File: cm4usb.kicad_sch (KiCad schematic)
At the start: 24 parts, among them J6 USB4110-GF-A, J7 USB4110-GF-A, U10 USB3740B-AI2, U11 AP22653FDZ-7

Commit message: respin
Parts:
- renumbered C20 to C22, C21 to C23, C22 to C24, C23 to C25, C24 to C26, C25 to C27, C26 to C28, C27 to C29, C28 to C30, C29 to C31, D8 to D7, R25 to R28, R26 to R29, R27 to R30, R28 to R31, R29 to R32, R30 to R33, R31 to R34, R32 to R35, R33 to R36, U10 to U11, U11 to U12
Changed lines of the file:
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@@
   (symbol (lib_id "Device:R_Small") (at 297.434 85.344 270) (unit 1)
     (in_bom yes) (on_board yes)
-    (property "Reference" "R32" (id 0) (at 297.434 87.63 90))
+    (property "Reference" "R35" (id 0) (at 297.434 87.63 90))
     (property "Value" "10k" (id 1) (at 297.434 90.17 90))
     (property "Footprint" "Resistor_SMD:R_0402_1005Metric" (id 2) (at 297.434 85.344 0)
@@
   (symbol (lib_id "Device:R_Small") (at 203.2 254 90) (unit 1)
     (in_bom yes) (on_board yes)
-    (property "Reference" "R30" (id 0) (at 196.85 252.73 90)
+    (property "Reference" "R33" (id 0) (at 196.85 252.73 90)
       (effects (font (size 1.27 1.27)) (justify right))
     )
@@
   (symbol (lib_id "Device:C_Small") (at 337.82 82.55 0) (unit 1)
     (in_bom yes) (on_board yes)
-    (property "Reference" "C26" (id 0) (at 339.09 81.28 0)
+    (property "Reference" "C28" (id 0) (at 339.09 81.28 0)
       (effects (font (size 1.27 1.27)) (justify left))
     )
@@
   (symbol (lib_id "Device:R_Small") (at 142.24 128.27 90) (unit 1)
     (in_bom yes) (on_board yes)
-    (property "Reference" "R28" (id 0) (at 145.034 131.064 90)
+    (property "Reference" "R31" (id 0) (at 145.034 131.064 90)
       (effects (font (size 1.27 1.27)) (justify left))
     )
@@
   (symbol (lib_id "Device:LED_Small") (at 149.86 102.87 90) (unit 1)
     (in_bom yes) (on_board yes)
-    (property "Reference" "D8" (id 0) (at 146.685 104.14 0)
+    (property "Reference" "D7" (id 0) (at 146.685 104.14 0)
       (effects (font (size 1.27 1.27)) (justify left))
     )
@@
   (symbol (lib_id "Device:C_Small") (at 327.66 82.55 0) (unit 1)
     (in_bom yes) (on_board yes)
-    (property "Reference" "C25" (id 0) (at 328.93 81.28 0)
+    (property "Reference" "C27" (id 0) (at 328.93 81.28 0)
       (effects (font (size 1.27 1.27)) (justify left))
     )
@@
   (symbol (lib_id "power:GND") (at 368.3 94.742 0) (unit 1)
     (in_bom yes) (on_board yes)
-    (property "Reference" "#PWR036" (id 0) (at 368.3 101.092 0)
+    (property "Reference" "#PWR037" (id 0) (at 368.3 101.092 0)
       (effects (font (size 1.27 1.27)) hide)
     )
@@
   (symbol (lib_id "Device:R_Small") (at 142.24 87.63 270) (unit 1)
     (in_bom yes) (on_board yes)
-    (property "Reference" "R27" (id 0) (at 139.7 82.55 90)
+    (property "Reference" "R30" (id 0) (at 139.7 82.55 90)
       (effects (font (size 1.27 1.27)) (justify left))
     )
@@
   (symbol (lib_id "Device:C_Small") (at 347.98 82.55 0) (unit 1)
     (in_bom yes) (on_board yes)
-    (property "Reference" "C27" (id 0) (at 349.25 81.28 0)
+    (property "Reference" "C29" (id 0) (at 349.25 81.28 0)
       (effects (font (size 1.27 1.27)) (justify left))
     )
@@
   (symbol (lib_id "Device:C_Small") (at 358.14 82.55 0) (unit 1)
     (in_bom yes) (on_board yes)
-    (property "Reference" "C28" (id 0) (at 359.41 81.28 0)
+    (property "Reference" "C30" (id 0) (at 359.41 81.28 0)
       (effects (font (size 1.27 1.27)) (justify left))
     )
@@
   (symbol (lib_id "Device:C_Small") (at 203.2 259.08 90) (unit 1)
     (in_bom yes) (on_board yes)
-    (property "Reference" "C23" (id 0) (at 196.85 257.81 90)
+    (property "Reference" "C25" (id 0) (at 196.85 257.81 90)
       (effects (font (size 1.27 1.27)) (justify right))
     )
@@
   (symbol (lib_id "Device:C_Small") (at 368.3 82.55 0) (unit 1)
     (in_bom yes) (on_board yes)
-    (property "Reference" "C29" (id 0) (at 369.57 81.28 0)
+    (property "Reference" "C31" (id 0) (at 369.57 81.28 0)
       (effects (font (size 1.27 1.27)) (justify left))
     )
@@
   (symbol (lib_id "power:GND") (at 106.68 151.13 0) (unit 1)
     (in_bom yes) (on_board yes)
-    (property "Reference" "#PWR033" (id 0) (at 106.68 157.48 0)
+    (property "Reference" "#PWR034" (id 0) (at 106.68 157.48 0)
       (effects (font (size 1.27 1.27)) hide)
     )
@@
   (symbol (lib_id "Device:R_Small") (at 207.01 218.44 90) (unit 1)
     (in_bom yes) (on_board yes)
-    (property "Reference" "R31" (id 0) (at 201.93 217.17 90))
+    (property "Reference" "R34" (id 0) (at 201.93 217.17 90))
     (property "Value" "5.1k" (id 1) (at 212.09 217.17 90))
     (property "Footprint" "Resistor_SMD:R_0402_1005Metric" (id 2) (at 207.01 218.44 0)
@@
   (symbol (lib_id "Device:R_Small") (at 80.01 254 90) (unit 1)
     (in_bom yes) (on_board yes)
-    (property "Reference" "R25" (id 0) (at 73.66 252.73 90)
+    (property "Reference" "R28" (id 0) (at 73.66 252.73 90)
       (effects (font (size 1.27 1.27)) (justify right))
     )
@@
   (symbol (lib_id "Device:R_Small") (at 82.55 218.44 90) (unit 1)
     (in_bom yes) (on_board yes)
-    (property "Reference" "R26" (id 0) (at 77.47 217.17 90))
+    (property "Reference" "R29" (id 0) (at 77.47 217.17 90))
     (property "Value" "5.1k" (id 1) (at 87.63 217.17 90))
     (property "Footprint" "Resistor_SMD:R_0402_1005Metric" (id 2) (at 82.55 218.44 0)
@@
   (symbol (lib_id "power:GND") (at 95.25 262.89 0) (unit 1)
     (in_bom yes) (on_board yes)
-    (property "Reference" "#PWR032" (id 0) (at 95.25 269.24 0)
+    (property "Reference" "#PWR033" (id 0) (at 95.25 269.24 0)
       (effects (font (size 1.27 1.27)) hide)
     )
@@
   (symbol (lib_id "power:GND") (at 149.86 151.13 0) (unit 1)
     (in_bom yes) (on_board yes)
-    (property "Reference" "#PWR034" (id 0) (at 149.86 157.48 0)
+    (property "Reference" "#PWR035" (id 0) (at 149.86 157.48 0)
       (effects (font (size 1.27 1.27)) hide)
     )
@@
   (symbol (lib_id "Power_Protection_Diodes:AP22653FDZ-7") (at 297.18 78.74 0) (unit 1)
     (in_bom yes) (on_board yes)
-    (property "Reference" "U11" (id 0) (at 297.18 69.85 0))
+    (property "Reference" "U12" (id 0) (at 297.18 69.85 0))
     (property "Value" "AP22653FDZ-7" (id 1) (at 297.18 72.39 0))
     (property "Footprint" "Power_Protection_Diodes:Diodes_W-DFN2020-6_A1" (id 2) (at 297.18 92.71 0)
@@
   (symbol (lib_id "Interface_USB_Microchip:USB3740B-AI2") (at 121.285 116.84 0) (unit 1)
     (in_bom yes) (on_board yes)
-    (property "Reference" "U10" (id 0) (at 121.92 102.87 0))
+    (property "Reference" "U11" (id 0) (at 121.92 102.87 0))
     (property "Value" "USB3740B-AI2" (id 1) (at 121.92 105.41 0))
     (property "Footprint" "Interface_USB_Microchip:Microchip_UQFN-10_1.3x1.8mm_P0.4mm_pin1" (id 2) (at 121.285 149.86 0)
@@
   (symbol (lib_id "Device:C_Small") (at 80.01 259.08 90) (unit 1)
     (in_bom yes) (on_board yes)
-    (property "Reference" "C20" (id 0) (at 73.66 257.81 90)
+    (property "Reference" "C22" (id 0) (at 73.66 257.81 90)
       (effects (font (size 1.27 1.27)) (justify right))
     )
@@
   (symbol (lib_id "Device:C_Small") (at 85.09 130.81 0) (mirror y) (unit 1)
     (in_bom yes) (on_board yes) (fields_autoplaced)
-    (property "Reference" "C21" (id 0) (at 82.55 129.54 0)
+    (property "Reference" "C23" (id 0) (at 82.55 129.54 0)
       (effects (font (size 1.27 1.27)) (justify left))
     )
@@
   (symbol (lib_id "Device:R_Small") (at 316.23 78.74 90) (unit 1)
     (in_bom yes) (on_board yes)
-    (property "Reference" "R33" (id 0) (at 318.77 81.28 90)
+    (property "Reference" "R36" (id 0) (at 318.77 81.28 90)
       (effects (font (size 1.27 1.27)) (justify left))
     )
@@
   (symbol (lib_id "power:GND") (at 219.71 262.89 0) (unit 1)
     (in_bom yes) (on_board yes)
-    (property "Reference" "#PWR035" (id 0) (at 219.71 269.24 0)
+    (property "Reference" "#PWR036" (id 0) (at 219.71 269.24 0)
       (effects (font (size 1.27 1.27)) hide)
     )
@@
   (symbol (lib_id "Device:C_Small") (at 267.97 81.28 0) (unit 1)
     (in_bom yes) (on_board yes)
-    (property "Reference" "C24" (id 0) (at 269.24 80.01 0)
+    (property "Reference" "C26" (id 0) (at 269.24 80.01 0)
       (effects (font (size 1.27 1.27)) (justify left))
     )
@@
   (symbol (lib_id "power:PWR_FLAG") (at 168.91 279.4 0) (unit 1)
     (in_bom yes) (on_board yes) (fields_autoplaced)
-    (property "Reference" "#FLG07" (id 0) (at 168.91 277.495 0)
+    (property "Reference" "#FLG05" (id 0) (at 168.91 277.495 0)
       (effects (font (size 1.27 1.27)) hide)
     )
@@
   (symbol (lib_id "Device:C_Small") (at 96.52 130.81 0) (mirror y) (unit 1)
     (in_bom yes) (on_board yes) (fields_autoplaced)
-    (property "Reference" "C22" (id 0) (at 93.98 129.54 0)
+    (property "Reference" "C24" (id 0) (at 93.98 129.54 0)
       (effects (font (size 1.27 1.27)) (justify left))
     )
@@
   (symbol (lib_id "Device:R_Small") (at 149.86 92.71 0) (mirror x) (unit 1)
     (in_bom yes) (on_board yes)
-    (property "Reference" "R29" (id 0) (at 151.384 91.44 0)
+    (property "Reference" "R32" (id 0) (at 151.384 91.44 0)
       (effects (font (size 1.27 1.27)) (justify left))
     )
@@
   (symbol (lib_id "power:GND") (at 85.09 138.43 0) (mirror y) (unit 1)
     (in_bom yes) (on_board yes)
-    (property "Reference" "#PWR031" (id 0) (at 85.09 144.78 0)
-      (effects (font (size 1.27 1.27)) hide)
-    )
+    (property "Reference" "#PWR032" (id 0) (at 85.09 144.78 0)
+      (effects (font (size 1.27 1.27)) hide)
+    )

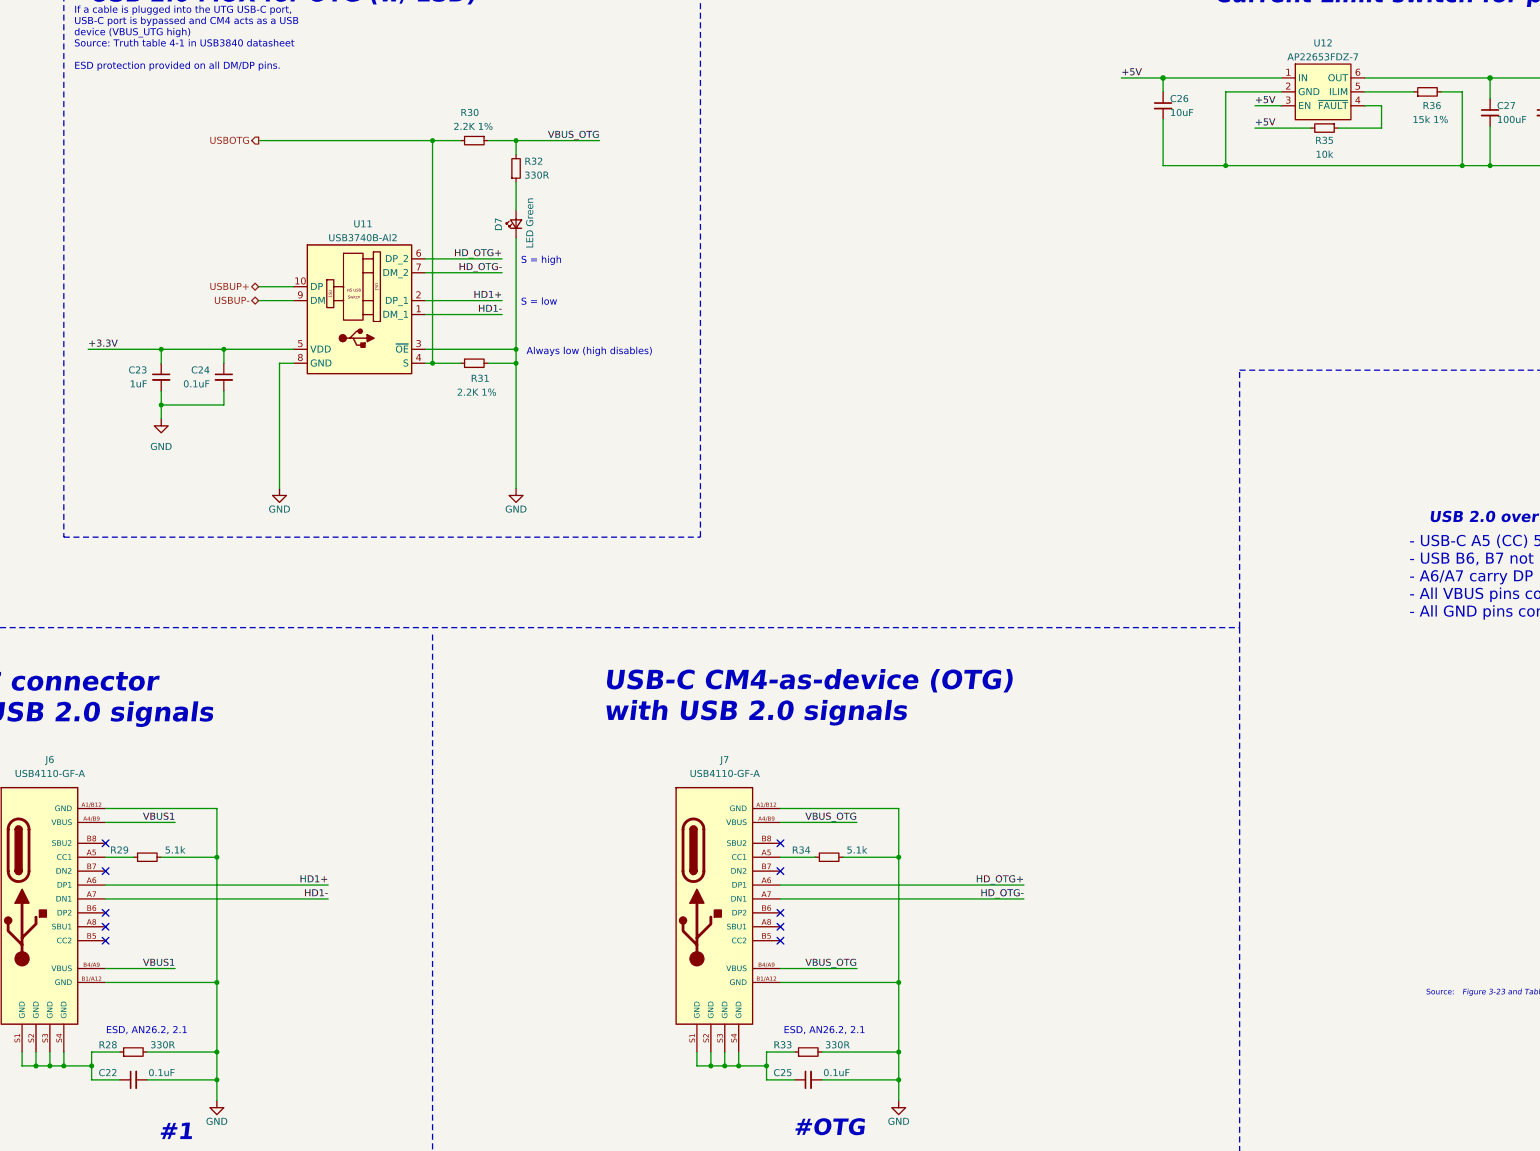
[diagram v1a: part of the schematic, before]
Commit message: fixed I2C ping indicator
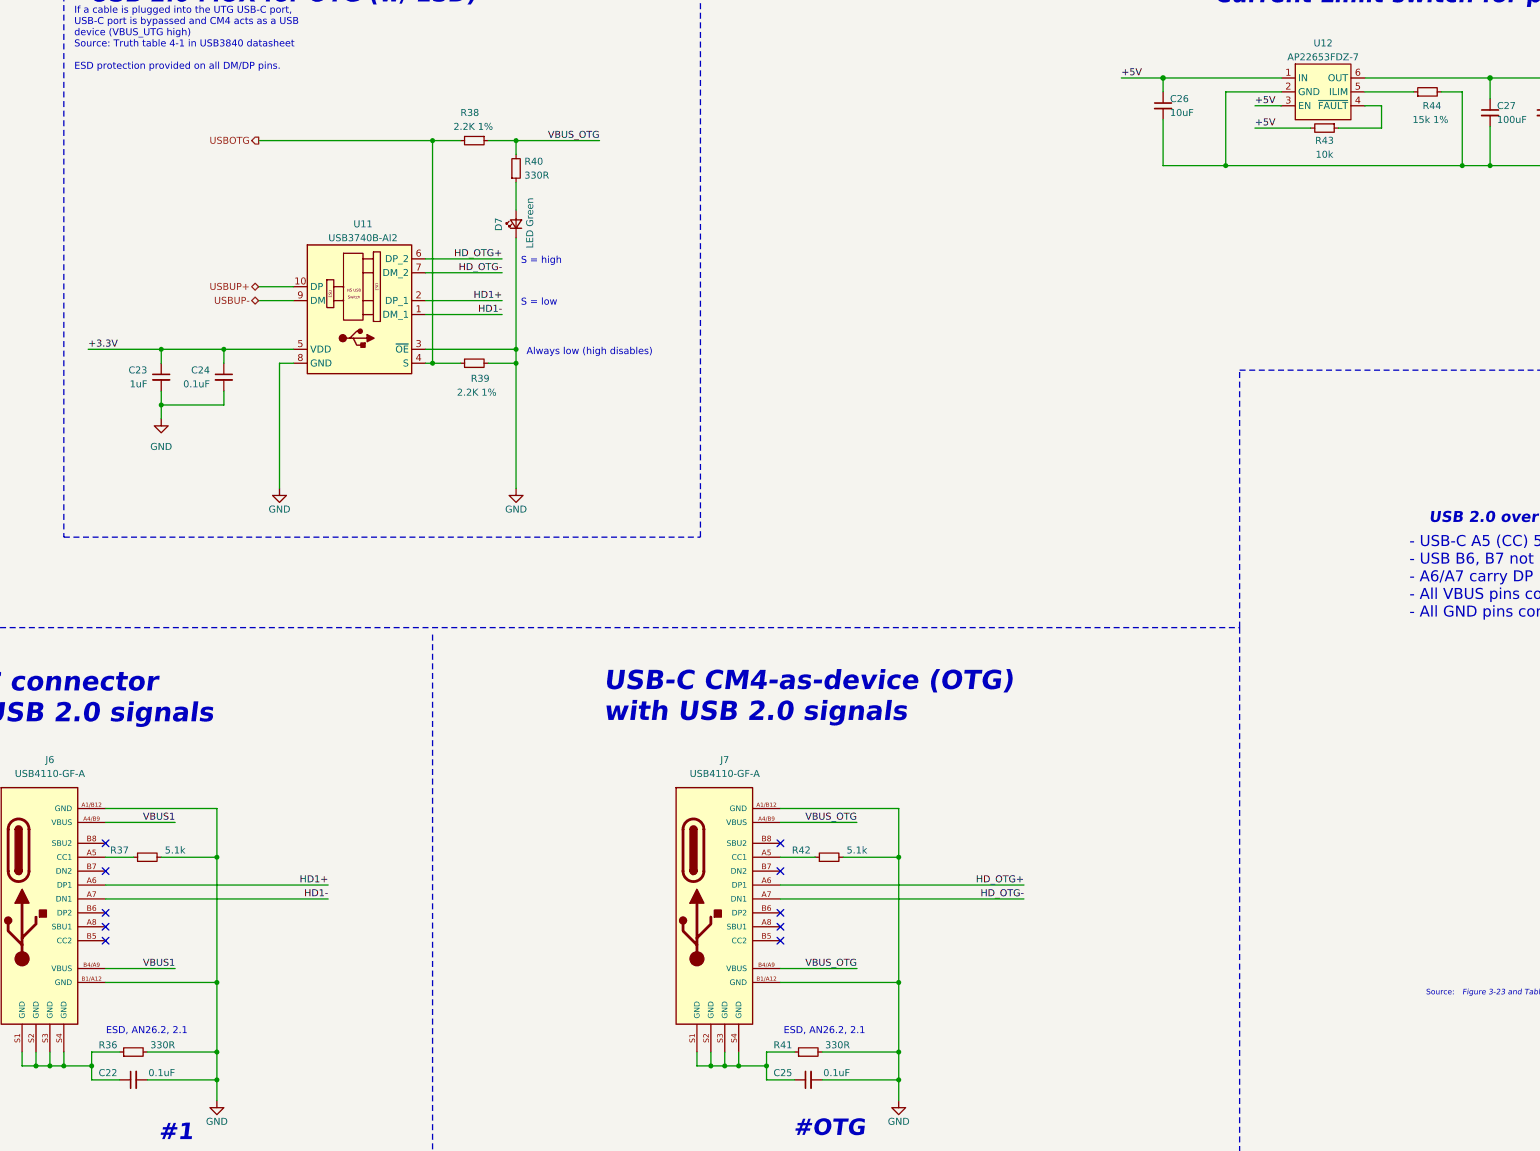
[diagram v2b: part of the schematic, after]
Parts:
- renumbered R28 to R36, R29 to R37, R30 to R38, R31 to R39, R32 to R40, R33 to R41, R34 to R42, R35 to R43, R36 to R44
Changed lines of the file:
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@@
   (symbol (lib_id "Device:R_Small") (at 297.434 85.344 270) (unit 1)
     (in_bom yes) (on_board yes)
-    (property "Reference" "R35" (id 0) (at 297.434 87.63 90))
+    (property "Reference" "R43" (id 0) (at 297.434 87.63 90))
     (property "Value" "10k" (id 1) (at 297.434 90.17 90))
     (property "Footprint" "Resistor_SMD:R_0402_1005Metric" (id 2) (at 297.434 85.344 0)
@@
   (symbol (lib_id "Device:R_Small") (at 203.2 254 90) (unit 1)
     (in_bom yes) (on_board yes)
-    (property "Reference" "R33" (id 0) (at 196.85 252.73 90)
+    (property "Reference" "R41" (id 0) (at 196.85 252.73 90)
       (effects (font (size 1.27 1.27)) (justify right))
     )
@@
   (symbol (lib_id "Device:R_Small") (at 142.24 128.27 90) (unit 1)
     (in_bom yes) (on_board yes)
-    (property "Reference" "R31" (id 0) (at 145.034 131.064 90)
+    (property "Reference" "R39" (id 0) (at 145.034 131.064 90)
       (effects (font (size 1.27 1.27)) (justify left))
     )
@@
   (symbol (lib_id "power:GND") (at 368.3 94.742 0) (unit 1)
     (in_bom yes) (on_board yes)
-    (property "Reference" "#PWR037" (id 0) (at 368.3 101.092 0)
+    (property "Reference" "#PWR039" (id 0) (at 368.3 101.092 0)
       (effects (font (size 1.27 1.27)) hide)
     )
@@
   (symbol (lib_id "Device:R_Small") (at 142.24 87.63 270) (unit 1)
     (in_bom yes) (on_board yes)
-    (property "Reference" "R30" (id 0) (at 139.7 82.55 90)
+    (property "Reference" "R38" (id 0) (at 139.7 82.55 90)
       (effects (font (size 1.27 1.27)) (justify left))
     )
@@
   (symbol (lib_id "power:GND") (at 106.68 151.13 0) (unit 1)
     (in_bom yes) (on_board yes)
-    (property "Reference" "#PWR034" (id 0) (at 106.68 157.48 0)
+    (property "Reference" "#PWR036" (id 0) (at 106.68 157.48 0)
       (effects (font (size 1.27 1.27)) hide)
     )
@@
   (symbol (lib_id "Device:R_Small") (at 207.01 218.44 90) (unit 1)
     (in_bom yes) (on_board yes)
-    (property "Reference" "R34" (id 0) (at 201.93 217.17 90))
+    (property "Reference" "R42" (id 0) (at 201.93 217.17 90))
     (property "Value" "5.1k" (id 1) (at 212.09 217.17 90))
     (property "Footprint" "Resistor_SMD:R_0402_1005Metric" (id 2) (at 207.01 218.44 0)
@@
   (symbol (lib_id "Device:R_Small") (at 80.01 254 90) (unit 1)
     (in_bom yes) (on_board yes)
-    (property "Reference" "R28" (id 0) (at 73.66 252.73 90)
+    (property "Reference" "R36" (id 0) (at 73.66 252.73 90)
       (effects (font (size 1.27 1.27)) (justify right))
     )
@@
   (symbol (lib_id "Device:R_Small") (at 82.55 218.44 90) (unit 1)
     (in_bom yes) (on_board yes)
-    (property "Reference" "R29" (id 0) (at 77.47 217.17 90))
+    (property "Reference" "R37" (id 0) (at 77.47 217.17 90))
     (property "Value" "5.1k" (id 1) (at 87.63 217.17 90))
     (property "Footprint" "Resistor_SMD:R_0402_1005Metric" (id 2) (at 82.55 218.44 0)
@@
   (symbol (lib_id "power:GND") (at 95.25 262.89 0) (unit 1)
     (in_bom yes) (on_board yes)
-    (property "Reference" "#PWR033" (id 0) (at 95.25 269.24 0)
+    (property "Reference" "#PWR035" (id 0) (at 95.25 269.24 0)
       (effects (font (size 1.27 1.27)) hide)
     )
@@
   (symbol (lib_id "power:GND") (at 149.86 151.13 0) (unit 1)
     (in_bom yes) (on_board yes)
-    (property "Reference" "#PWR035" (id 0) (at 149.86 157.48 0)
+    (property "Reference" "#PWR037" (id 0) (at 149.86 157.48 0)
       (effects (font (size 1.27 1.27)) hide)
     )
@@
   (symbol (lib_id "Device:R_Small") (at 316.23 78.74 90) (unit 1)
     (in_bom yes) (on_board yes)
-    (property "Reference" "R36" (id 0) (at 318.77 81.28 90)
+    (property "Reference" "R44" (id 0) (at 318.77 81.28 90)
       (effects (font (size 1.27 1.27)) (justify left))
     )
@@
   (symbol (lib_id "power:GND") (at 219.71 262.89 0) (unit 1)
     (in_bom yes) (on_board yes)
-    (property "Reference" "#PWR036" (id 0) (at 219.71 269.24 0)
+    (property "Reference" "#PWR038" (id 0) (at 219.71 269.24 0)
       (effects (font (size 1.27 1.27)) hide)
     )
@@
   (symbol (lib_id "Device:R_Small") (at 149.86 92.71 0) (mirror x) (unit 1)
     (in_bom yes) (on_board yes)
-    (property "Reference" "R32" (id 0) (at 151.384 91.44 0)
+    (property "Reference" "R40" (id 0) (at 151.384 91.44 0)
       (effects (font (size 1.27 1.27)) (justify left))
     )
@@
   (symbol (lib_id "power:GND") (at 85.09 138.43 0) (mirror y) (unit 1)
     (in_bom yes) (on_board yes)
-    (property "Reference" "#PWR032" (id 0) (at 85.09 144.78 0)
-      (effects (font (size 1.27 1.27)) hide)
-    )
+    (property "Reference" "#PWR034" (id 0) (at 85.09 144.78 0)
+      (effects (font (size 1.27 1.27)) hide)
+    )
